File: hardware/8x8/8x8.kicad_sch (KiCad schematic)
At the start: 10 parts

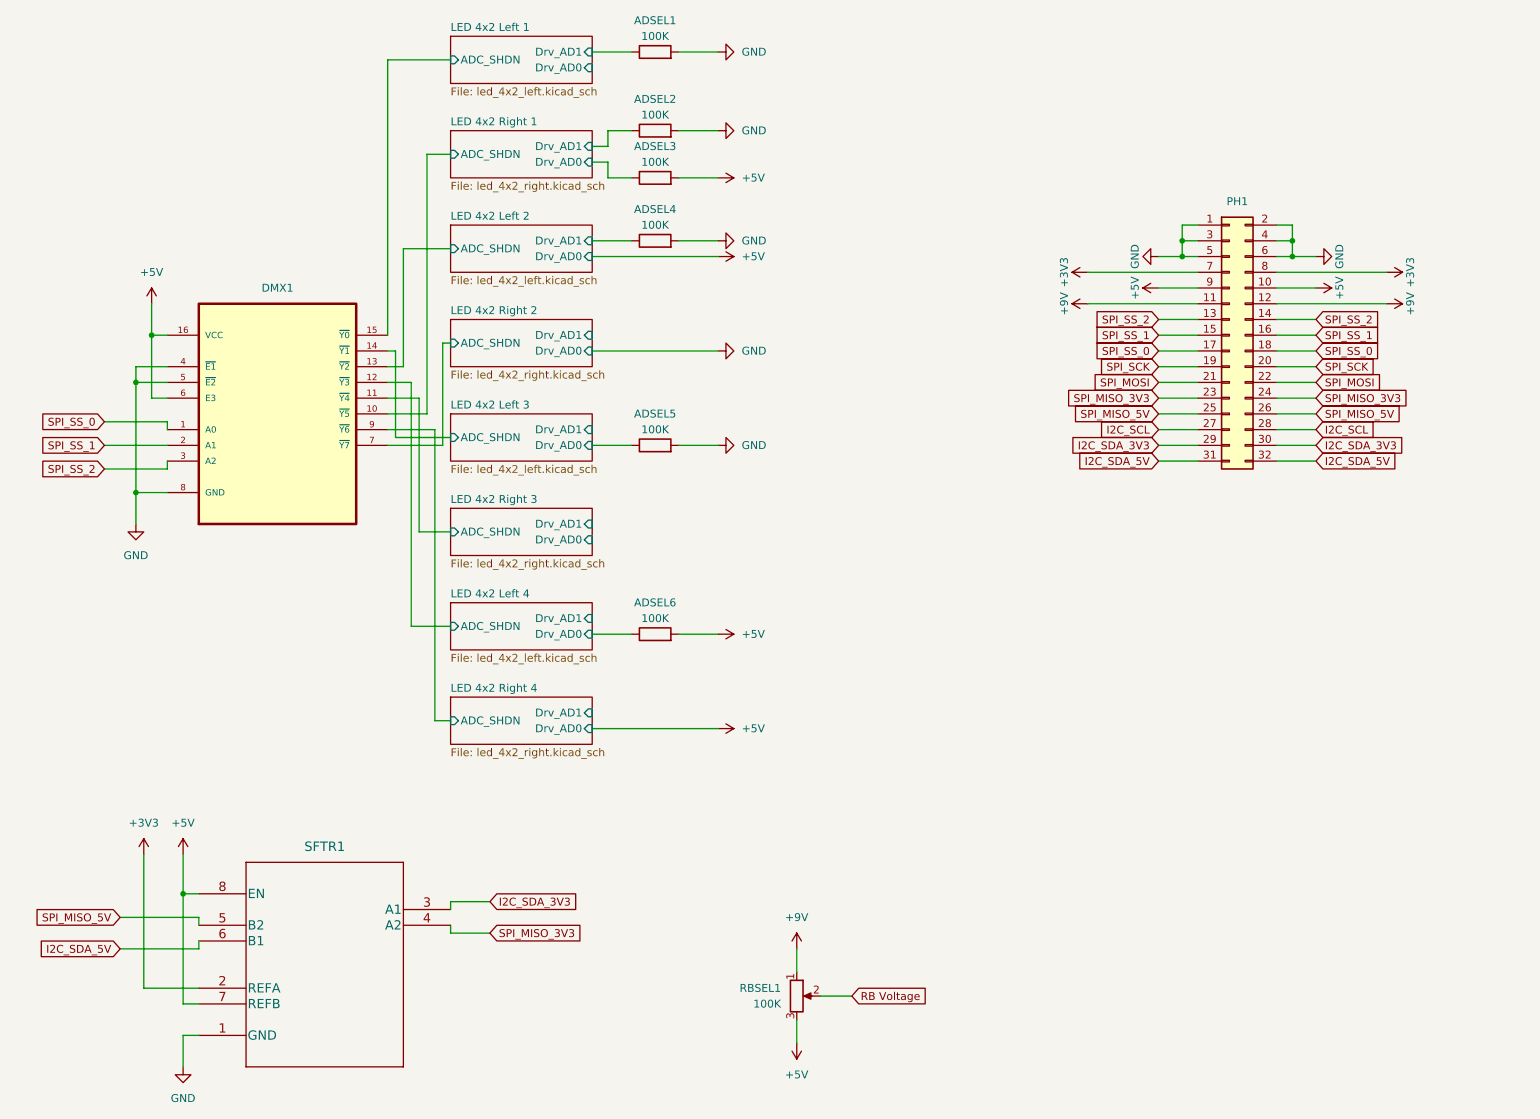
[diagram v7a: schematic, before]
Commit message: Updated Trace Widths and Ground Fill
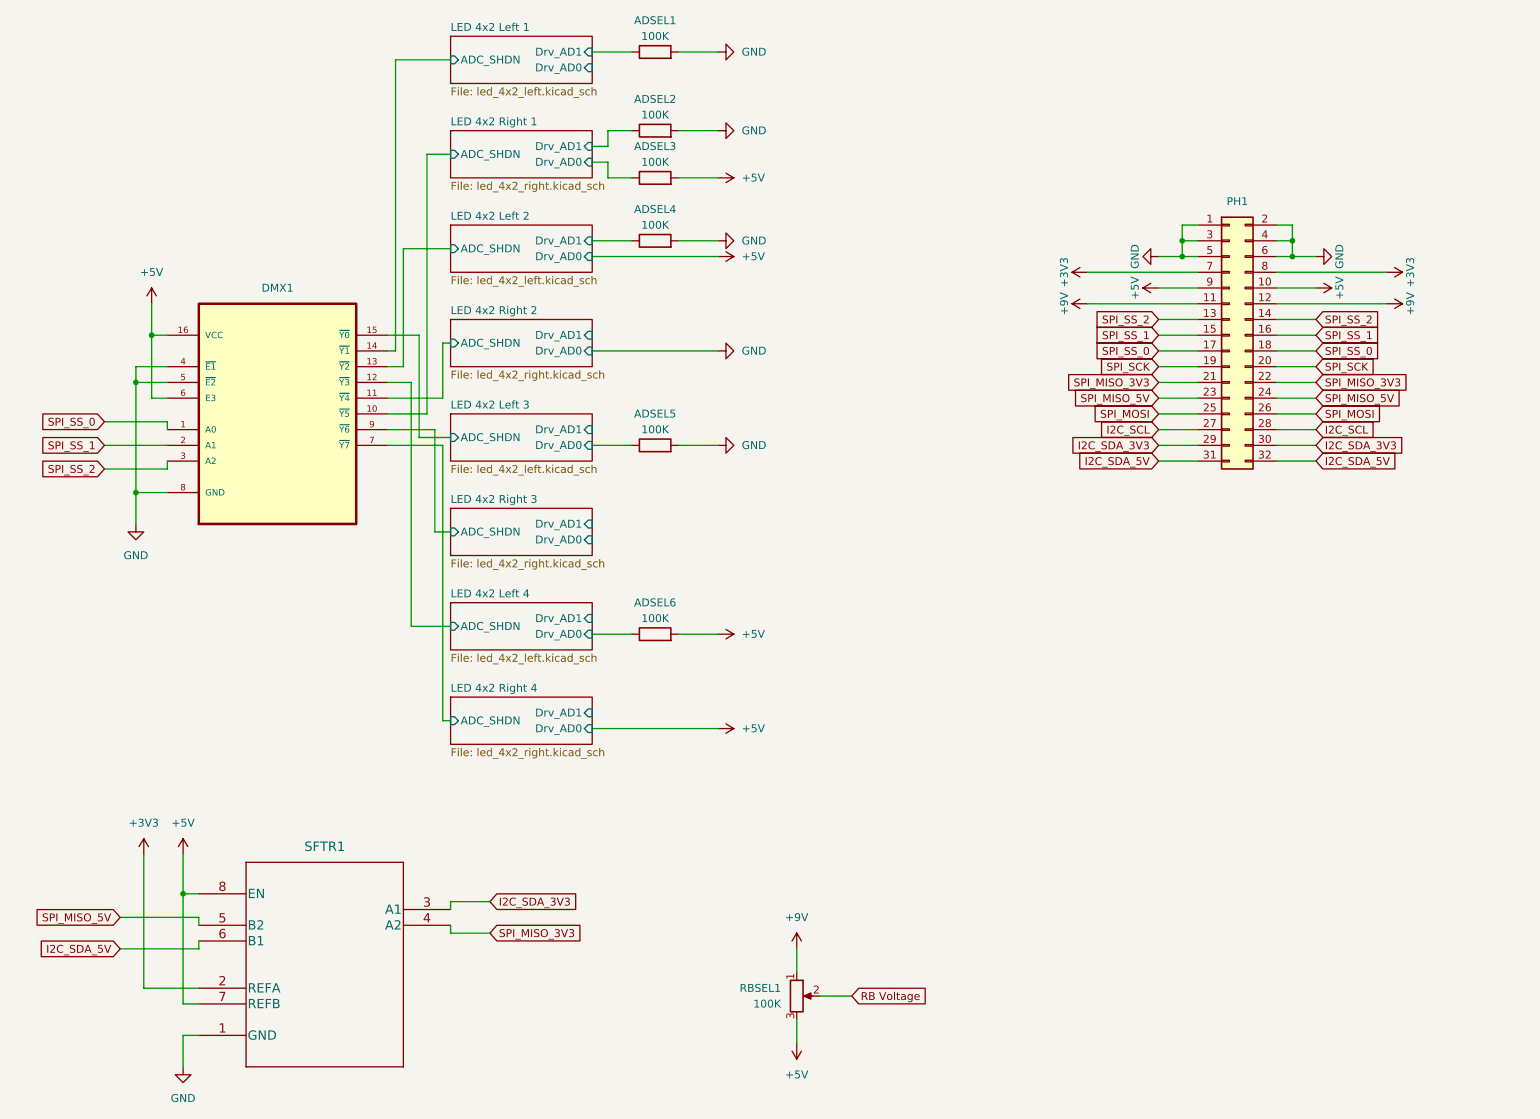
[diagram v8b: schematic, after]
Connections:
- net LED 4x2 Left 1/ADC_SHDN: now also DMX1.14 (~{Y1}); no longer DMX1.15 (~{Y0})
- net LED 4x2 Left 3/ADC_SHDN: now also DMX1.15 (~{Y0}); no longer DMX1.14 (~{Y1})
- net LED 4x2 Right 2/ADC_SHDN: now also DMX1.11 (~{Y4}); no longer DMX1.7 (~{Y7})
- net LED 4x2 Right 3/ADC_SHDN: now also DMX1.9 (~{Y6}); no longer DMX1.11 (~{Y4})
- net LED 4x2 Right 4/ADC_SHDN: now also DMX1.7 (~{Y7}); no longer DMX1.9 (~{Y6})
- net SPI_MISO_3V3: now also PH1.21 (Pin_21), PH1.22 (Pin_22); no longer PH1.23 (Pin_23), PH1.24 (Pin_24)
- net SPI_MISO_5V: now also PH1.23 (Pin_23), PH1.24 (Pin_24); no longer PH1.25 (Pin_25), PH1.26 (Pin_26)
- net SPI_MOSI: now also PH1.25 (Pin_25), PH1.26 (Pin_26); no longer PH1.21 (Pin_21), PH1.22 (Pin_22)
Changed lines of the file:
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@@
-    (stroke (width 0) (type default) (color 0 0 0 0))
-  )
-  (wire (pts (xy 73.66 69.85) (xy 73.66 83.82))
     (stroke (width 0) (type default) (color 0 0 0 0))
   )
@@
     (stroke (width 0) (type default) (color 0 0 0 0))
   )
+  (wire (pts (xy 82.55 83.82) (xy 77.47 83.82))
+    (stroke (width 0) (type default) (color 0 0 0 0))
+  )
   (wire (pts (xy 107.95 34.29) (xy 107.95 36.83))
     (stroke (width 0) (type default) (color 0 0 0 0))
   )
-  (wire (pts (xy 77.47 77.47) (xy 77.47 99.06))
-    (stroke (width 0) (type default) (color 0 0 0 0))
-  )
   (wire (pts (xy 203.2 57.15) (xy 185.42 57.15))
     (stroke (width 0) (type default) (color 0 0 0 0))
@@
     (stroke (width 0) (type default) (color 0 0 0 0))
   )
+  (wire (pts (xy 81.28 77.47) (xy 81.28 68.58))
+    (stroke (width 0) (type default) (color 0 0 0 0))
+  )
   (wire (pts (xy 218.44 54.61) (xy 222.25 54.61))
     (stroke (width 0) (type default) (color 0 0 0 0))
@@
     (stroke (width 0) (type default) (color 0 0 0 0))
   )
-  (wire (pts (xy 77.47 99.06) (xy 82.55 99.06))
+  (wire (pts (xy 77.47 83.82) (xy 77.47 67.31))
     (stroke (width 0) (type default) (color 0 0 0 0))
   )
@@
     (stroke (width 0) (type default) (color 0 0 0 0))
   )
+  (wire (pts (xy 81.28 85.09) (xy 81.28 129.54))
+    (stroke (width 0) (type default) (color 0 0 0 0))
+  )
   (wire (pts (xy 34.29 62.23) (xy 34.29 67.31))
     (stroke (width 0) (type default) (color 0 0 0 0))
@@
     (stroke (width 0) (type default) (color 0 0 0 0))
   )
+  (wire (pts (xy 73.66 22.86) (xy 82.55 22.86))
+    (stroke (width 0) (type default) (color 0 0 0 0))
+  )
   (wire (pts (xy 200.66 52.07) (xy 200.66 54.61))
     (stroke (width 0) (type default) (color 0 0 0 0))
@@
     (stroke (width 0) (type default) (color 0 0 0 0))
   )
-  (wire (pts (xy 80.01 82.55) (xy 80.01 129.54))
-    (stroke (width 0) (type default) (color 0 0 0 0))
-  )
   (wire (pts (xy 215.9 77.47) (xy 222.25 77.47))
     (stroke (width 0) (type default) (color 0 0 0 0))
@@
     (stroke (width 0) (type default) (color 0 0 0 0))
   )
-  (wire (pts (xy 72.39 67.31) (xy 72.39 22.86))
-    (stroke (width 0) (type default) (color 0 0 0 0))
-  )
   (wire (pts (xy 72.39 72.39) (xy 74.93 72.39))
     (stroke (width 0) (type default) (color 0 0 0 0))
@@
     (stroke (width 0) (type default) (color 0 0 0 0))
   )
-  (wire (pts (xy 80.01 129.54) (xy 82.55 129.54))
-    (stroke (width 0) (type default) (color 0 0 0 0))
-  )
   (wire (pts (xy 105.41 85.09) (xy 111.76 85.09))
     (stroke (width 0) (type default) (color 0 0 0 0))
@@
     (stroke (width 0) (type default) (color 0 0 0 0))
   )
-  (wire (pts (xy 72.39 77.47) (xy 77.47 77.47))
+  (wire (pts (xy 81.28 129.54) (xy 82.55 129.54))
     (stroke (width 0) (type default) (color 0 0 0 0))
   )
@@
     (stroke (width 0) (type default) (color 0 0 0 0))
   )
-  (wire (pts (xy 81.28 68.58) (xy 81.28 85.09))
-    (stroke (width 0) (type default) (color 0 0 0 0))
-  )
   (wire (pts (xy 203.2 69.85) (xy 196.85 69.85))
     (stroke (width 0) (type default) (color 0 0 0 0))
@@
     (stroke (width 0) (type default) (color 0 0 0 0))
   )
+  (wire (pts (xy 72.39 77.47) (xy 81.28 77.47))
+    (stroke (width 0) (type default) (color 0 0 0 0))
+  )
   (wire (pts (xy 82.55 158.75) (xy 82.55 160.02))
     (stroke (width 0) (type default) (color 0 0 0 0))
@@
     (stroke (width 0) (type default) (color 0 0 0 0))
   )
+  (wire (pts (xy 73.66 69.85) (xy 73.66 22.86))
+    (stroke (width 0) (type default) (color 0 0 0 0))
+  )
   (wire (pts (xy 222.25 87.63) (xy 215.9 87.63))
     (stroke (width 0) (type default) (color 0 0 0 0))
   )
-  (wire (pts (xy 73.66 83.82) (xy 82.55 83.82))
-    (stroke (width 0) (type default) (color 0 0 0 0))
-  )
   (wire (pts (xy 31.75 74.93) (xy 36.83 74.93))
     (stroke (width 0) (type default) (color 0 0 0 0))
@@
     (stroke (width 0) (type default) (color 0 0 0 0))
   )
-  (wire (pts (xy 72.39 22.86) (xy 82.55 22.86))
-    (stroke (width 0) (type default) (color 0 0 0 0))
-  )
   (wire (pts (xy 72.39 74.93) (xy 76.2 74.93))
     (stroke (width 0) (type default) (color 0 0 0 0))
@@
     (stroke (width 0) (type default) (color 0 0 0 0))
   )
+  (wire (pts (xy 80.01 99.06) (xy 82.55 99.06))
+    (stroke (width 0) (type default) (color 0 0 0 0))
+  )
   (wire (pts (xy 203.2 80.01) (xy 196.85 80.01))
     (stroke (width 0) (type default) (color 0 0 0 0))
@@
     (stroke (width 0) (type default) (color 0 0 0 0))
   )
+  (wire (pts (xy 77.47 67.31) (xy 72.39 67.31))
+    (stroke (width 0) (type default) (color 0 0 0 0))
+  )
+  (wire (pts (xy 80.01 82.55) (xy 80.01 99.06))
+    (stroke (width 0) (type default) (color 0 0 0 0))
+  )
   (wire (pts (xy 81.28 85.09) (xy 72.39 85.09))
     (stroke (width 0) (type default) (color 0 0 0 0))
@@
     (stroke (width 0) (type default) (color 0 0 0 0))
   )
-  (global_label "SPI_MISO_3V3" (shape input) (at 222.25 77.47 0) (fields_autoplaced)
-    (effects (font (size 1.27 1.27)) (justify left))
-    (property "Intersheet References" "${INTERSHEET_REFS}" (id 0) (at 237.7864 77.3906 0)
-      (effects (font (size 1.27 1.27)) (justify left) hide)
-    )
-  )
   (global_label "I2C_SDA_5V" (shape input) (at 29.21 166.37 180) (fields_autoplaced)
     (effects (font (size 1.27 1.27)) (justify right))
@@
     )
   )
+  (global_label "SPI_MOSI" (shape input) (at 222.25 80.01 0) (fields_autoplaced)
+    (effects (font (size 1.27 1.27)) (justify left))
+    (property "Intersheet References" "${INTERSHEET_REFS}" (id 0) (at 233.3112 79.9306 0)
+      (effects (font (size 1.27 1.27)) (justify left) hide)
+    )
+  )
   (global_label "SPI_SS_2" (shape input) (at 196.85 64.77 180) (fields_autoplaced)
     (effects (font (size 1.27 1.27)) (justify right))
@@
     )
   )
-  (global_label "SPI_MISO_3V3" (shape input) (at 196.85 77.47 180) (fields_autoplaced)
-    (effects (font (size 1.27 1.27)) (justify right))
-    (property "Intersheet References" "${INTERSHEET_REFS}" (id 0) (at 181.3136 77.3906 0)
-      (effects (font (size 1.27 1.27)) (justify right) hide)
-    )
-  )
-  (global_label "SPI_MISO_5V" (shape input) (at 222.25 80.01 0) (fields_autoplaced)
-    (effects (font (size 1.27 1.27)) (justify left))
-    (property "Intersheet References" "${INTERSHEET_REFS}" (id 0) (at 236.5769 79.9306 0)
-      (effects (font (size 1.27 1.27)) (justify left) hide)
-    )
-  )
   (global_label "I2C_SCL" (shape input) (at 196.85 82.55 180) (fields_autoplaced)
     (effects (font (size 1.27 1.27)) (justify right))
@@
     )
   )
-  (global_label "SPI_MISO_5V" (shape input) (at 196.85 80.01 180) (fields_autoplaced)
-    (effects (font (size 1.27 1.27)) (justify right))
-    (property "Intersheet References" "${INTERSHEET_REFS}" (id 0) (at 182.5231 79.9306 0)
-      (effects (font (size 1.27 1.27)) (justify right) hide)
-    )
-  )
-  (global_label "SPI_MOSI" (shape input) (at 222.25 74.93 0) (fields_autoplaced)
-    (effects (font (size 1.27 1.27)) (justify left))
-    (property "Intersheet References" "${INTERSHEET_REFS}" (id 0) (at 233.3112 74.8506 0)
-      (effects (font (size 1.27 1.27)) (justify left) hide)
-    )
-  )
   (global_label "SPI_MISO_5V" (shape input) (at 29.21 161.29 180) (fields_autoplaced)
     (effects (font (size 1.27 1.27)) (justify right))
@@
     )
   )
-  (global_label "SPI_MOSI" (shape input) (at 196.85 74.93 180) (fields_autoplaced)
-    (effects (font (size 1.27 1.27)) (justify right))
-    (property "Intersheet References" "${INTERSHEET_REFS}" (id 0) (at 185.7888 74.8506 0)
-      (effects (font (size 1.27 1.27)) (justify right) hide)
-    )
-  )
   (global_label "I2C_SCL" (shape input) (at 222.25 82.55 0) (fields_autoplaced)
     (effects (font (size 1.27 1.27)) (justify left))
@@
     )
   )
+  (global_label "SPI_MISO_5V" (shape input) (at 222.25 77.47 0) (fields_autoplaced)
+    (effects (font (size 1.27 1.27)) (justify left))
+    (property "Intersheet References" "${INTERSHEET_REFS}" (id 0) (at 236.5769 77.3906 0)
+      (effects (font (size 1.27 1.27)) (justify left) hide)
+    )
+  )
   (global_label "SPI_SS_0" (shape input) (at 222.25 69.85 0) (fields_autoplaced)
     (effects (font (size 1.27 1.27)) (justify left))
@@
     )
   )
+  (global_label "SPI_MISO_3V3" (shape input) (at 196.85 74.93 180) (fields_autoplaced)
+    (effects (font (size 1.27 1.27)) (justify right))
+    (property "Intersheet References" "${INTERSHEET_REFS}" (id 0) (at 181.3136 74.8506 0)
+      (effects (font (size 1.27 1.27)) (justify right) hide)
+    )
+  )
+  (global_label "SPI_MISO_5V" (shape input) (at 196.85 77.47 180) (fields_autoplaced)
+    (effects (font (size 1.27 1.27)) (justify right))
+    (property "Intersheet References" "${INTERSHEET_REFS}" (id 0) (at 182.5231 77.3906 0)
+      (effects (font (size 1.27 1.27)) (justify right) hide)
+    )
+  )
   (global_label "SPI_MISO_3V3" (shape input) (at 88.9 163.83 0) (fields_autoplaced)
     (effects (font (size 1.27 1.27)) (justify left))
@@
       (effects (font (size 1.27 1.27)) (justify right) hide)
     )
+  )
+  (global_label "SPI_MISO_3V3" (shape input) (at 222.25 74.93 0) (fields_autoplaced)
+    (effects (font (size 1.27 1.27)) (justify left))
+    (property "Intersheet References" "${INTERSHEET_REFS}" (id 0) (at 237.7864 74.8506 0)
+      (effects (font (size 1.27 1.27)) (justify left) hide)
+    )
+  )
+  (global_label "SPI_MOSI" (shape input) (at 196.85 80.01 180) (fields_autoplaced)
+    (effects (font (size 1.27 1.27)) (justify right))
+    (property "Intersheet References" "${INTERSHEET_REFS}" (id 0) (at 185.7888 79.9306 0)
+      (effects (font (size 1.27 1.27)) (justify right) hide)
+    )
